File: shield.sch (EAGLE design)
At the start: 12 parts

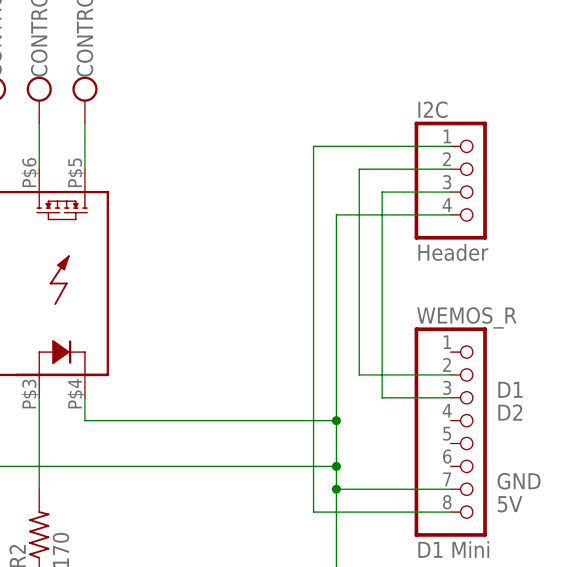
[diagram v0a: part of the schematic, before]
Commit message: Tweak layout and add lables
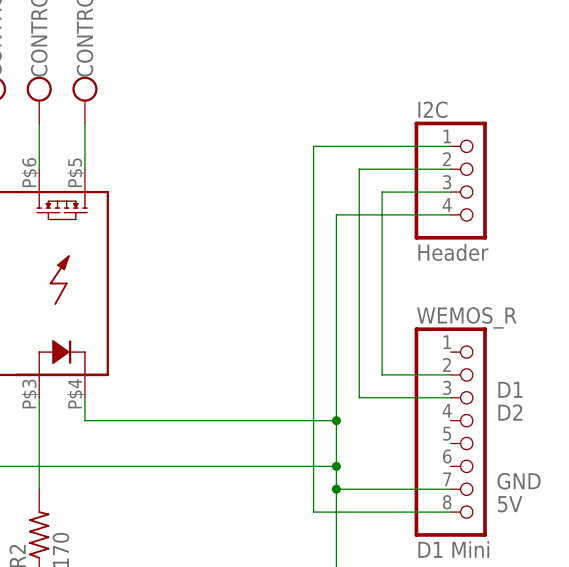
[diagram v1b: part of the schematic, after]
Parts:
- R5, R6: MPN (none) -> CRCW060310K0JNEBC
- U$1: MPN (none) -> TLP206GA(F)
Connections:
- net D1: now also WEMOS_R.3; no longer WEMOS_R.2
- net D2: now also WEMOS_R.2; no longer WEMOS_R.3

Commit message: tweak silkscreen and add some missing files
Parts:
- CONTROL, SENSORS: device con-ptr500:AK550/4 -> shield:AK550/4
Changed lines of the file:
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@@
 <grid distance="0.1" unitdist="inch" unit="inch" style="lines" multiple="1" display="no" altdistance="0.01" altunitdist="inch" altunit="inch"/>
 <layers>
-<layer number="1" name="Top" color="4" fill="1" visible="yes" active="no"/>
-<layer number="16" name="Bottom" color="1" fill="1" visible="yes" active="no"/>
-<layer number="17" name="Pads" color="2" fill="1" visible="yes" active="no"/>
-<layer number="18" name="Vias" color="2" fill="1" visible="yes" active="no"/>
-<layer number="19" name="Unrouted" color="6" fill="1" visible="yes" active="no"/>
-<layer number="20" name="Dimension" color="24" fill="1" visible="yes" active="no"/>
-<layer number="21" name="tPlace" color="7" fill="1" visible="yes" active="no"/>
-<layer number="22" name="bPlace" color="7" fill="1" visible="yes" active="no"/>
-<layer number="23" name="tOrigins" color="15" fill="1" visible="yes" active="no"/>
-<layer number="24" name="bOrigins" color="15" fill="1" visible="yes" active="no"/>
-<layer number="25" name="tNames" color="7" fill="1" visible="yes" active="no"/>
-<layer number="26" name="bNames" color="7" fill="1" visible="yes" active="no"/>
-<layer number="27" name="tValues" color="7" fill="1" visible="yes" active="no"/>
-<layer number="28" name="bValues" color="7" fill="1" visible="yes" active="no"/>
+<layer number="1" name="Top" color="4" fill="1" visible="no" active="no"/>
+<layer number="16" name="Bottom" color="1" fill="1" visible="no" active="no"/>
+<layer number="17" name="Pads" color="2" fill="1" visible="no" active="no"/>
+<layer number="18" name="Vias" color="2" fill="1" visible="no" active="no"/>
+<layer number="19" name="Unrouted" color="6" fill="1" visible="no" active="no"/>
+<layer number="20" name="Dimension" color="24" fill="1" visible="no" active="no"/>
+<layer number="21" name="tPlace" color="7" fill="1" visible="no" active="no"/>
+<layer number="22" name="bPlace" color="7" fill="1" visible="no" active="no"/>
+<layer number="23" name="tOrigins" color="15" fill="1" visible="no" active="no"/>
+<layer number="24" name="bOrigins" color="15" fill="1" visible="no" active="no"/>
+<layer number="25" name="tNames" color="7" fill="1" visible="no" active="no"/>
+<layer number="26" name="bNames" color="7" fill="1" visible="no" active="no"/>
+<layer number="27" name="tValues" color="7" fill="1" visible="no" active="no"/>
+<layer number="28" name="bValues" color="7" fill="1" visible="no" active="no"/>
 <layer number="29" name="tStop" color="7" fill="3" visible="no" active="no"/>
 <layer number="30" name="bStop" color="7" fill="6" visible="no" active="no"/>
@@
 <layer number="35" name="tGlue" color="7" fill="4" visible="no" active="no"/>
 <layer number="36" name="bGlue" color="7" fill="5" visible="no" active="no"/>
-<layer number="37" name="tTest" color="7" fill="1" visible="yes" active="no"/>
-<layer number="38" name="bTest" color="7" fill="1" visible="yes" active="no"/>
+<layer number="37" name="tTest" color="7" fill="1" visible="no" active="no"/>
+<layer number="38" name="bTest" color="7" fill="1" visible="no" active="no"/>
 <layer number="39" name="tKeepout" color="4" fill="11" visible="no" active="no"/>
 <layer number="40" name="bKeepout" color="1" fill="11" visible="no" active="no"/>
@@
 <layer number="44" name="Drills" color="7" fill="1" visible="no" active="no"/>
 <layer number="45" name="Holes" color="7" fill="1" visible="no" active="no"/>
-<layer number="46" name="Milling" color="3" fill="1" visible="yes" active="no"/>
-<layer number="47" name="Measures" color="7" fill="1" visible="yes" active="no"/>
-<layer number="48" name="Document" color="7" fill="1" visible="yes" active="no"/>
-<layer number="49" name="Reference" color="7" fill="1" visible="yes" active="no"/>
-<layer number="50" name="dxf" color="7" fill="1" visible="yes" active="no"/>
-<layer number="51" name="tDocu" color="7" fill="1" visible="yes" active="no"/>
-<layer number="52" name="bDocu" color="7" fill="1" visible="yes" active="no"/>
-<layer number="53" name="tGND_GNDA" color="7" fill="1" visible="yes" active="no"/>
-<layer number="54" name="bGND_GNDA" color="7" fill="1" visible="yes" active="no"/>
-<layer number="56" name="wert" color="7" fill="1" visible="yes" active="no"/>
-<layer number="57" name="tCAD" color="7" fill="1" visible="yes" active="no"/>
-<layer number="59" name="tCarbon" color="7" fill="1" visible="yes" active="no"/>
-<layer number="60" name="bCarbon" color="7" fill="1" visible="yes" active="no"/>
+<layer number="46" name="Milling" color="3" fill="1" visible="no" active="no"/>
+<layer number="47" name="Measures" color="7" fill="1" visible="no" active="no"/>
+<layer number="48" name="Document" color="7" fill="1" visible="no" active="no"/>
+<layer number="49" name="Reference" color="7" fill="1" visible="no" active="no"/>
+<layer number="50" name="dxf" color="7" fill="1" visible="no" active="no"/>
+<layer number="51" name="tDocu" color="7" fill="1" visible="no" active="no"/>
+<layer number="52" name="bDocu" color="7" fill="1" visible="no" active="no"/>
+<layer number="53" name="tGND_GNDA" color="7" fill="1" visible="no" active="no"/>
+<layer number="54" name="bGND_GNDA" color="7" fill="1" visible="no" active="no"/>
+<layer number="56" name="wert" color="7" fill="1" visible="no" active="no"/>
+<layer number="57" name="tCAD" color="7" fill="1" visible="no" active="no"/>
+<layer number="59" name="tCarbon" color="7" fill="1" visible="no" active="no"/>
+<layer number="60" name="bCarbon" color="7" fill="1" visible="no" active="no"/>
 <layer number="88" name="SimResults" color="9" fill="1" visible="yes" active="yes"/>
 <layer number="89" name="SimProbes" color="9" fill="1" visible="yes" active="yes"/>
@@
 <attribute name="MPN" value="TLP206GA(F)"/>
 </part>
-<part name="CONTROL" library="con-ptr500" deviceset="AK550/4" device="" value="Screw"/>
-<part name="SENSORS" library="con-ptr500" deviceset="AK550/4" device="" value="Screw"/>
+<part name="CONTROL" library="shield" deviceset="AK550/4" device="" value="Screw"/>
+<part name="SENSORS" library="shield" deviceset="AK550/4" device="" value="Screw"/>
 <part name="R1" library="resistor" library_urn="urn:adsk.eagle:library:348" deviceset="R-US_" device="R0603" package3d_urn="urn:adsk.eagle:package:23555/3" value="170"/>
 <part name="R2" library="resistor" library_urn="urn:adsk.eagle:library:348" deviceset="R-US_" device="R0603" package3d_urn="urn:adsk.eagle:package:23555/3" value="170"/>

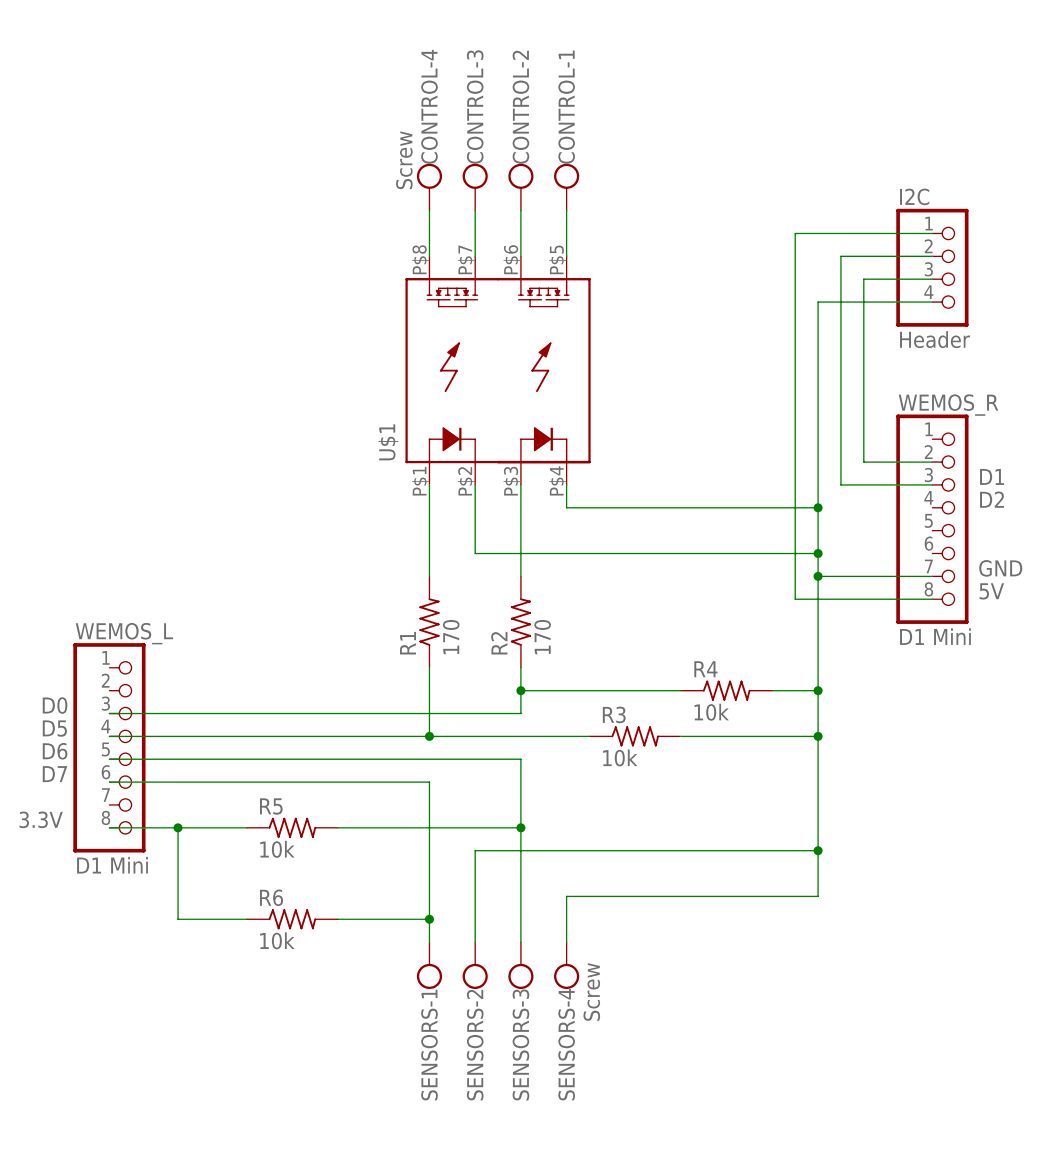
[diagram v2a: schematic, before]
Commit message: Changed to active low, changed chip, updated silkscreen
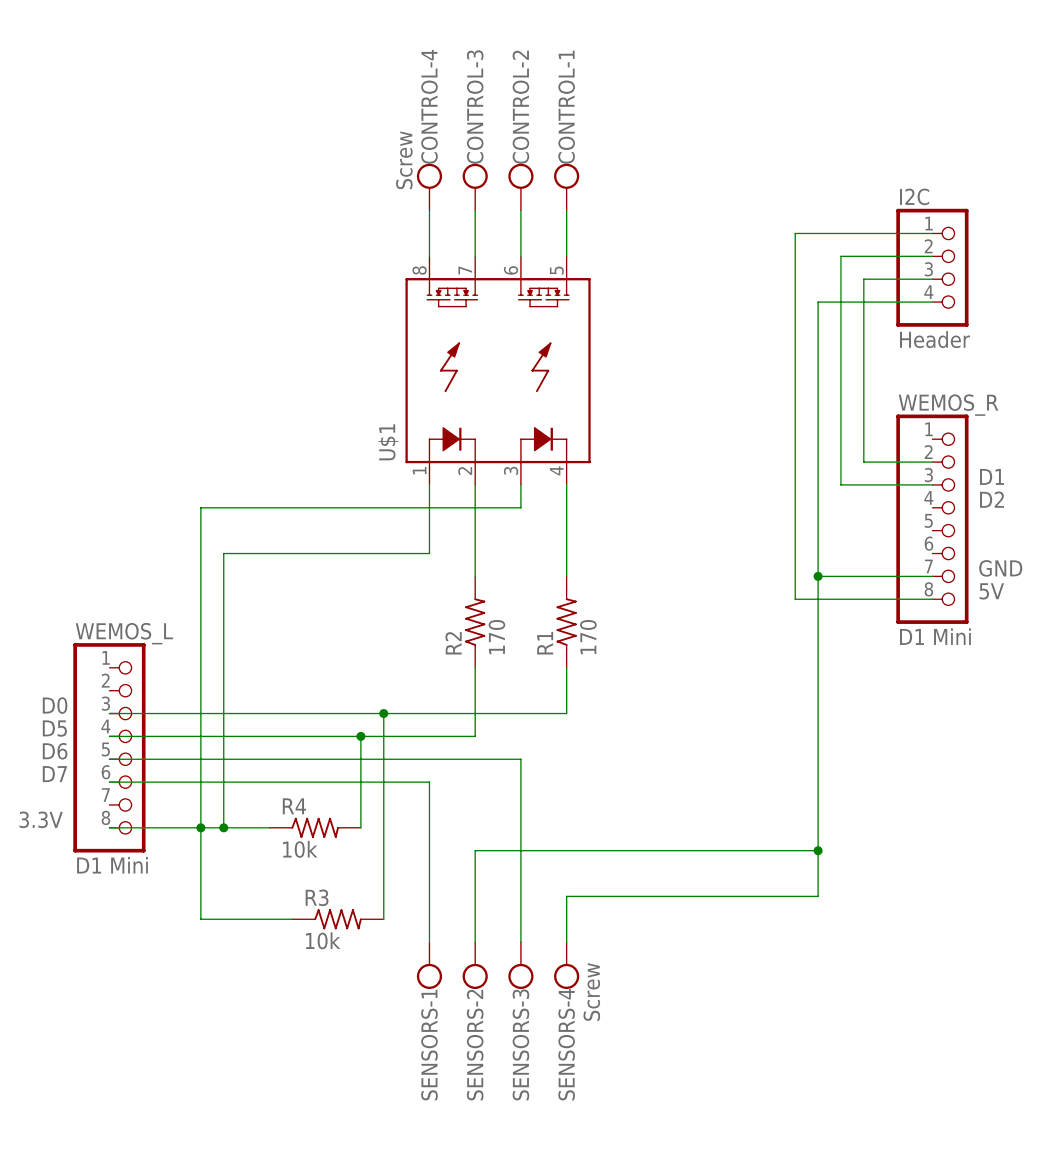
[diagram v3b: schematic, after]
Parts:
- removed R5, R6: 10k, resistor:R-US_R0603
- CONTROL, SENSORS: device shield:AK550/4 -> shield:AK550/4QUIET
- U$1: device ICCollection:TLP206A -> shield:TLP206A
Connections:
- net 3.3V: now also R3.1, R4.1, U$1.LED(+)_1, U$1.LED(+)_2; no longer R5.1, R6.1
- net D0: now also R1.1, R3.2; no longer R2.1, R4.1
- net D5: now also R2.1, R4.2; no longer R1.1, R3.1
- net D6: no longer R5.2
- net D7: no longer R6.2
- net GND: no longer R3.2, R4.2, U$1.LED(-)_1, U$1.LED(-)_2
- net N$4: now also R2.2, U$1.LED(-)_1; no longer R1.2, U$1.LED(+)_1
- net N$6: now also R1.2, U$1.LED(-)_2; no longer R2.2, U$1.LED(+)_2
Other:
- moved on the sheet: R1, R2, R3, R4

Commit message: Fix silkscreen for I2C, update values in schematic.
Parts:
- R1, R2: value 170 -> 220
- renumbered U$1 to TLP206GA(F)
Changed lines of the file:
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@@
 <part name="WEMOS_R" library="pinhead_v2" deviceset="PINHD-1X8" device="/OCT" value="D1 Mini"/>
 <part name="WEMOS_L" library="pinhead_v2" deviceset="PINHD-1X8" device="/OCT" value="D1 Mini"/>
-<part name="U$1" library="shield" deviceset="TLP206A" device="">
+<part name="TLP206GA(F)" library="shield" deviceset="TLP206A" device="">
 <attribute name="MPN" value="TLP206GA(F)"/>
 </part>
 <part name="CONTROL" library="shield" deviceset="AK550/4" device="QUIET" value="Screw"/>
 <part name="SENSORS" library="shield" deviceset="AK550/4" device="QUIET" value="Screw"/>
-<part name="R1" library="resistor" library_urn="urn:adsk.eagle:library:348" deviceset="R-US_" device="R0603" package3d_urn="urn:adsk.eagle:package:23555/3" value="170"/>
-<part name="R2" library="resistor" library_urn="urn:adsk.eagle:library:348" deviceset="R-US_" device="R0603" package3d_urn="urn:adsk.eagle:package:23555/3" value="170"/>
+<part name="R1" library="resistor" library_urn="urn:adsk.eagle:library:348" deviceset="R-US_" device="R0603" package3d_urn="urn:adsk.eagle:package:23555/3" value="220"/>
+<part name="R2" library="resistor" library_urn="urn:adsk.eagle:library:348" deviceset="R-US_" device="R0603" package3d_urn="urn:adsk.eagle:package:23555/3" value="220"/>
 <part name="R4" library="resistor" library_urn="urn:adsk.eagle:library:348" deviceset="R-US_" device="R0603" package3d_urn="urn:adsk.eagle:package:23555/3" value="10k"/>
 <part name="I2C" library="pinhead_v2" deviceset="PINHD-1X4" device="/OCT" value="Header"/>
@@
 <attribute name="VALUE" x="36.83" y="-2.54" size="1.778" layer="96"/>
 </instance>
-<instance part="U$1" gate="G$1" x="93.98" y="43.18" smashed="yes" rot="R90">
+<instance part="TLP206GA(F)" gate="G$1" x="93.98" y="43.18" smashed="yes" rot="R90">
 <attribute name="NAME" x="72.39" y="43.18" size="1.778" layer="95" font="vector" rot="R90"/>
 <attribute name="MPN" x="93.98" y="43.18" size="1.778" layer="96" rot="R90" display="off"/>
@@
 <segment>
 <pinref part="CONTROL" gate="-3" pin="KL"/>
-<pinref part="U$1" gate="G$1" pin="RELAY1_1"/>
+<pinref part="TLP206GA(F)" gate="G$1" pin="RELAY1_1"/>
 <wire x1="81.28" y1="71.12" x2="81.28" y2="66.04" width="0.1524" layer="91"/>
 </segment>
@@
 <segment>
 <pinref part="CONTROL" gate="-2" pin="KL"/>
-<pinref part="U$1" gate="G$1" pin="RELAY2_2"/>
+<pinref part="TLP206GA(F)" gate="G$1" pin="RELAY2_2"/>
 <wire x1="86.36" y1="71.12" x2="86.36" y2="66.04" width="0.1524" layer="91"/>
 </segment>
@@
 <pinref part="CONTROL" gate="-4" pin="KL"/>
 <wire x1="76.2" y1="71.12" x2="76.2" y2="66.04" width="0.1524" layer="91"/>
-<pinref part="U$1" gate="G$1" pin="RELAY1_2"/>
+<pinref part="TLP206GA(F)" gate="G$1" pin="RELAY1_2"/>
 </segment>
 </net>
@@
 <segment>
 <pinref part="CONTROL" gate="-1" pin="KL"/>
-<pinref part="U$1" gate="G$1" pin="RELAY2_1"/>
+<pinref part="TLP206GA(F)" gate="G$1" pin="RELAY2_1"/>
 <wire x1="91.44" y1="71.12" x2="91.44" y2="66.04" width="0.1524" layer="91"/>
 </segment>
@@
 <wire x1="58.42" y1="2.54" x2="53.34" y2="2.54" width="0.1524" layer="91"/>
 <junction x="53.34" y="2.54"/>
-<pinref part="U$1" gate="G$1" pin="LED(+)_1"/>
+<pinref part="TLP206GA(F)" gate="G$1" pin="LED(+)_1"/>
 <wire x1="76.2" y1="40.64" x2="76.2" y2="33.02" width="0.1524" layer="91"/>
-<pinref part="U$1" gate="G$1" pin="LED(+)_2"/>
+<pinref part="TLP206GA(F)" gate="G$1" pin="LED(+)_2"/>
 <wire x1="86.36" y1="40.64" x2="86.36" y2="38.1" width="0.1524" layer="91"/>
 </segment>
@@
 <net name="N$4" class="0">
 <segment>
-<pinref part="U$1" gate="G$1" pin="LED(-)_1"/>
+<pinref part="TLP206GA(F)" gate="G$1" pin="LED(-)_1"/>
 <pinref part="R2" gate="G$1" pin="2"/>
 <wire x1="81.28" y1="40.64" x2="81.28" y2="30.48" width="0.1524" layer="91"/>
@@
 <net name="N$6" class="0">
 <segment>
-<pinref part="U$1" gate="G$1" pin="LED(-)_2"/>
+<pinref part="TLP206GA(F)" gate="G$1" pin="LED(-)_2"/>
 <pinref part="R1" gate="G$1" pin="2"/>
 <wire x1="91.44" y1="40.64" x2="91.44" y2="30.48" width="0.1524" layer="91"/>
